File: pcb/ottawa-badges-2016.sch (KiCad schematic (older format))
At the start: 87 parts, among them P1 USB_OTG, P2 CONN_01X08, P3 CONN_01X06, P4 CONN_01X10, P5 CONN_01X08, P6 CONN_02X03, SW1 SWITCH_INV, SW2 SW_PUSH, U1 ATMEGA328P-A, U2 MIC5504-3.3YM5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

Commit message: Started layout of board.
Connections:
- net +3V3: now also P6.6 (P6); no longer P6.2 (P2)
- net DIGITAL12: now also P6.5 (P5); no longer P6.1 (P1)
- net GND: now also P6.2 (P2); no longer P6.6 (P6)
- net RESET: now also P6.1 (P1); no longer P6.5 (P5)
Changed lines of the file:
@@
 F 3 "" H 6750 2300 60  0000 C CNN
 	1    6750 3500
-	1    0    0    -1
+	1    0    0    1
 $EndComp
 $Comp

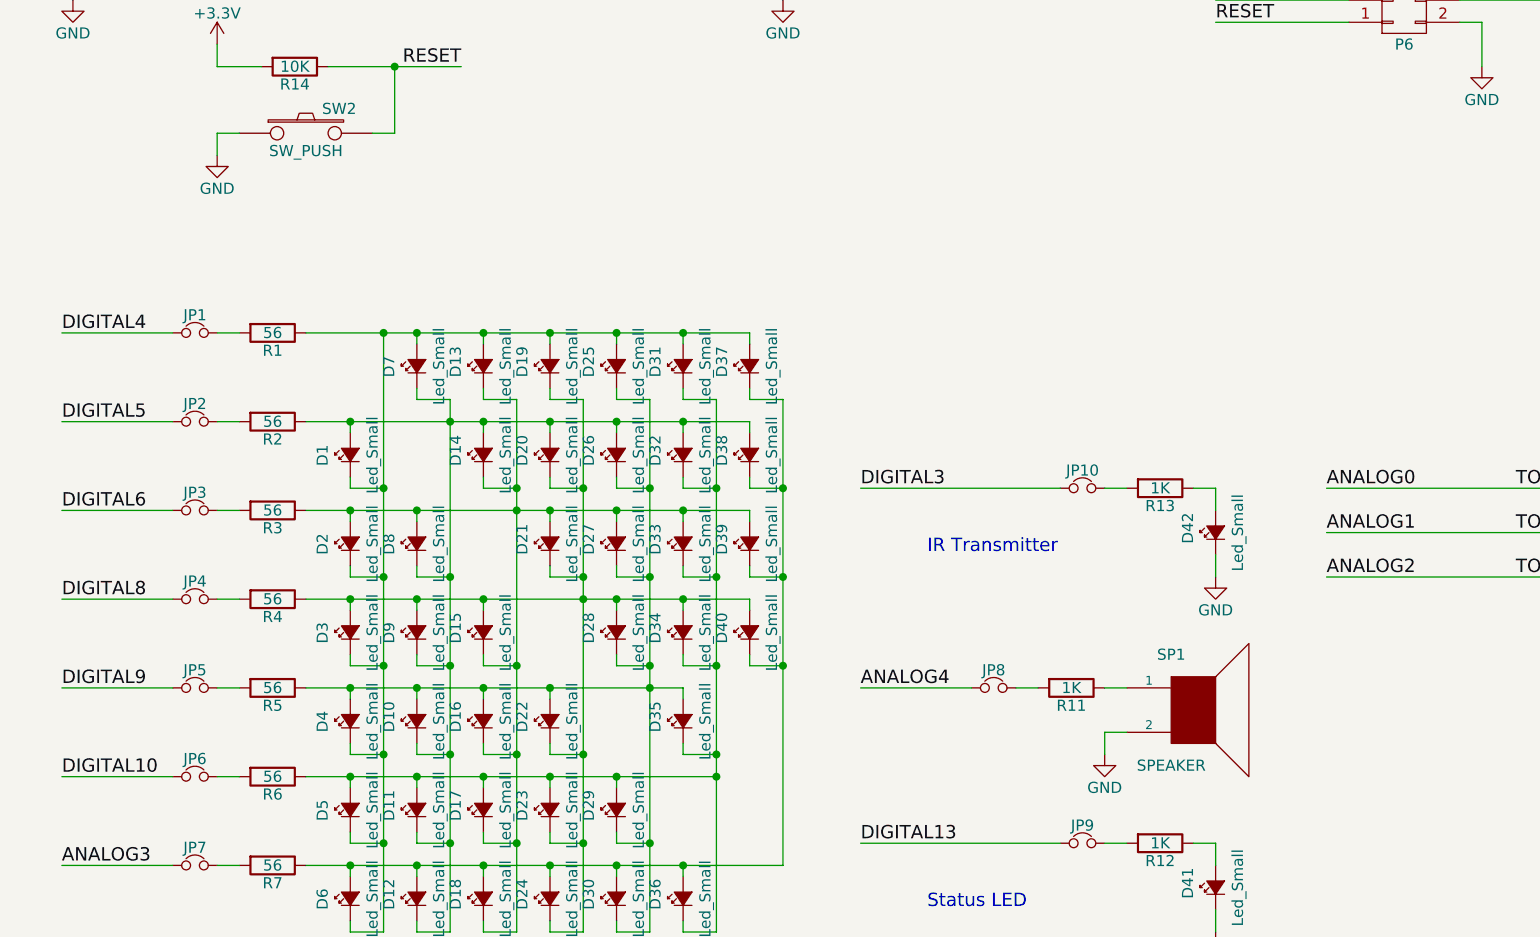
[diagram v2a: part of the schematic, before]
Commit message: MANY CHANGES. Added footprints for USB connector, battery clip, power switch, and solder jumper. Started adding banana jack "sockets".
Need to place the banana jacks, and add the IR receiver and artwork. Then I think we're done for the prototype.
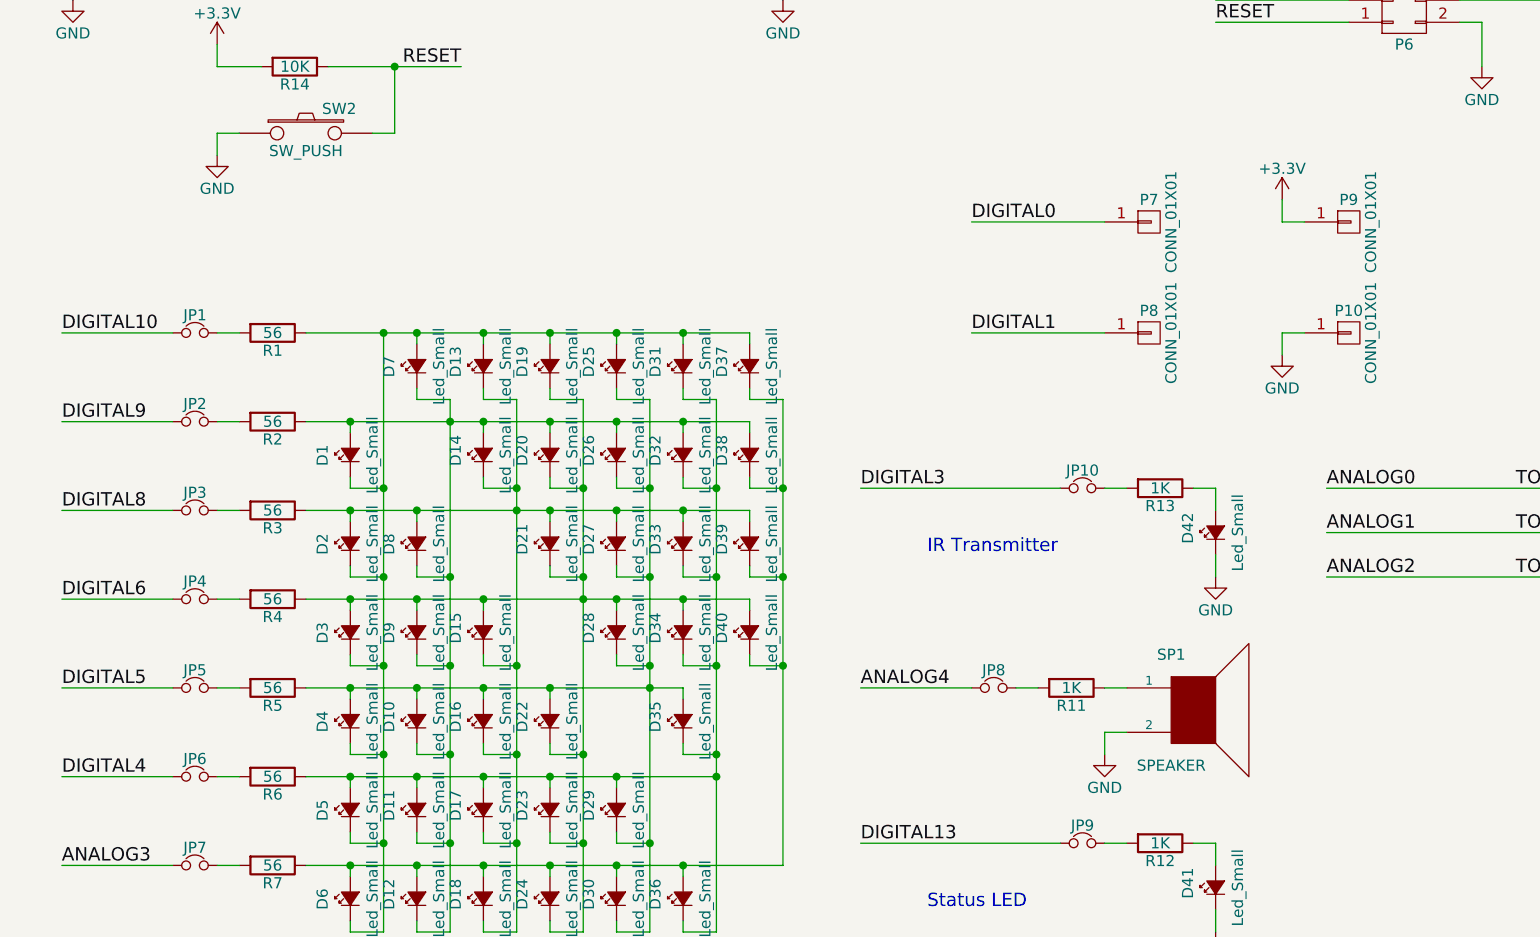
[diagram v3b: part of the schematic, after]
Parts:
- added P10, P7, P8, P9: CONN_01X01, Mounting_Holes:MountingHole_4mm_Pad_Via, symbol CONN_01X01
- BT1: footprint (none) -> BadgeParts:CR2032-SHRAPNEL
- JP1, JP10, JP2, JP3, JP4, JP5, JP6, JP7, JP8, JP9: footprint (none) -> BadgeParts:SJ2
- P1: footprint (none) -> BadgeParts:10118192-0001LF
- SW1: footprint (none) -> BadgeParts:MK-12C02
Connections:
- net +3V3: now also P9.1 (P1)
- net DIGITAL0: now also P7.1 (P1)
- net DIGITAL1: now also P8.1 (P1)
- net DIGITAL10: now also JP1.1; no longer JP6.1
- net DIGITAL4: now also JP6.1; no longer JP1.1
- net DIGITAL5: now also JP5.1; no longer JP2.1
- net DIGITAL6: now also JP4.1; no longer JP3.1
- net DIGITAL8: now also JP3.1; no longer JP4.1
- net DIGITAL9: now also JP2.1; no longer JP5.1
- net GND: now also P10.1 (P1)

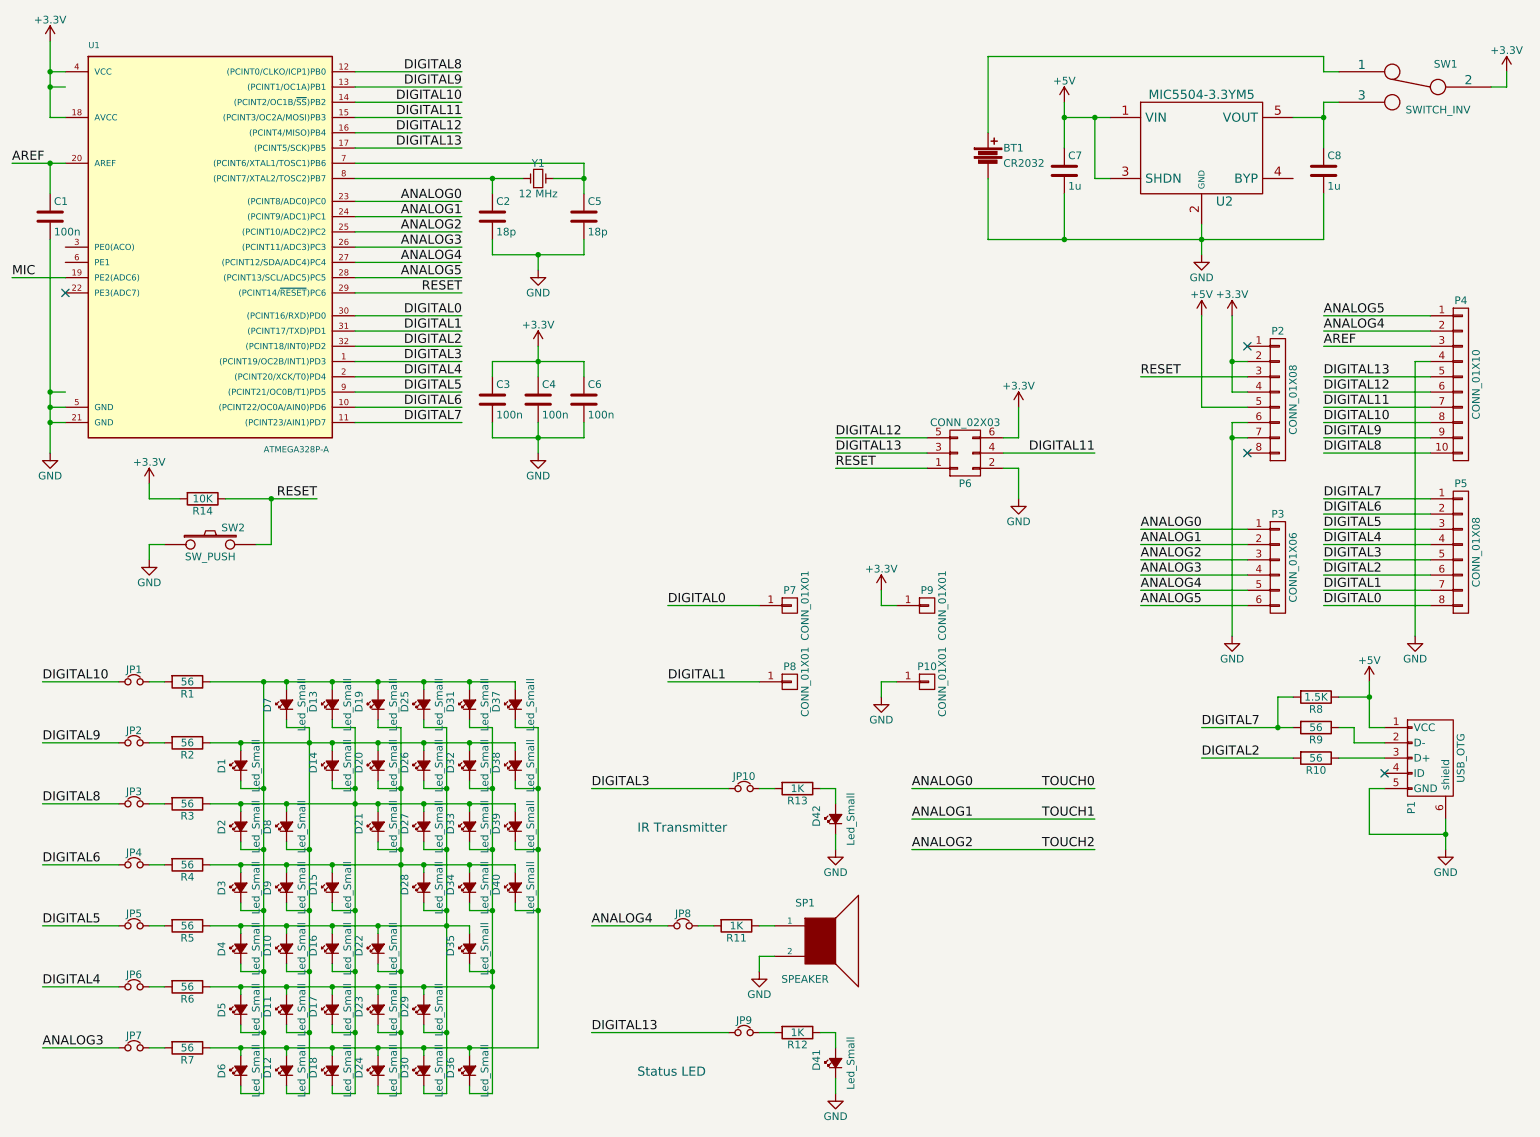
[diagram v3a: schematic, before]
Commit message: Added IR receiver and Maker Faire logo. Still need to add Makey for prototype. Also need to figure out where to put P8 so that it doesn't overlap with the logo.
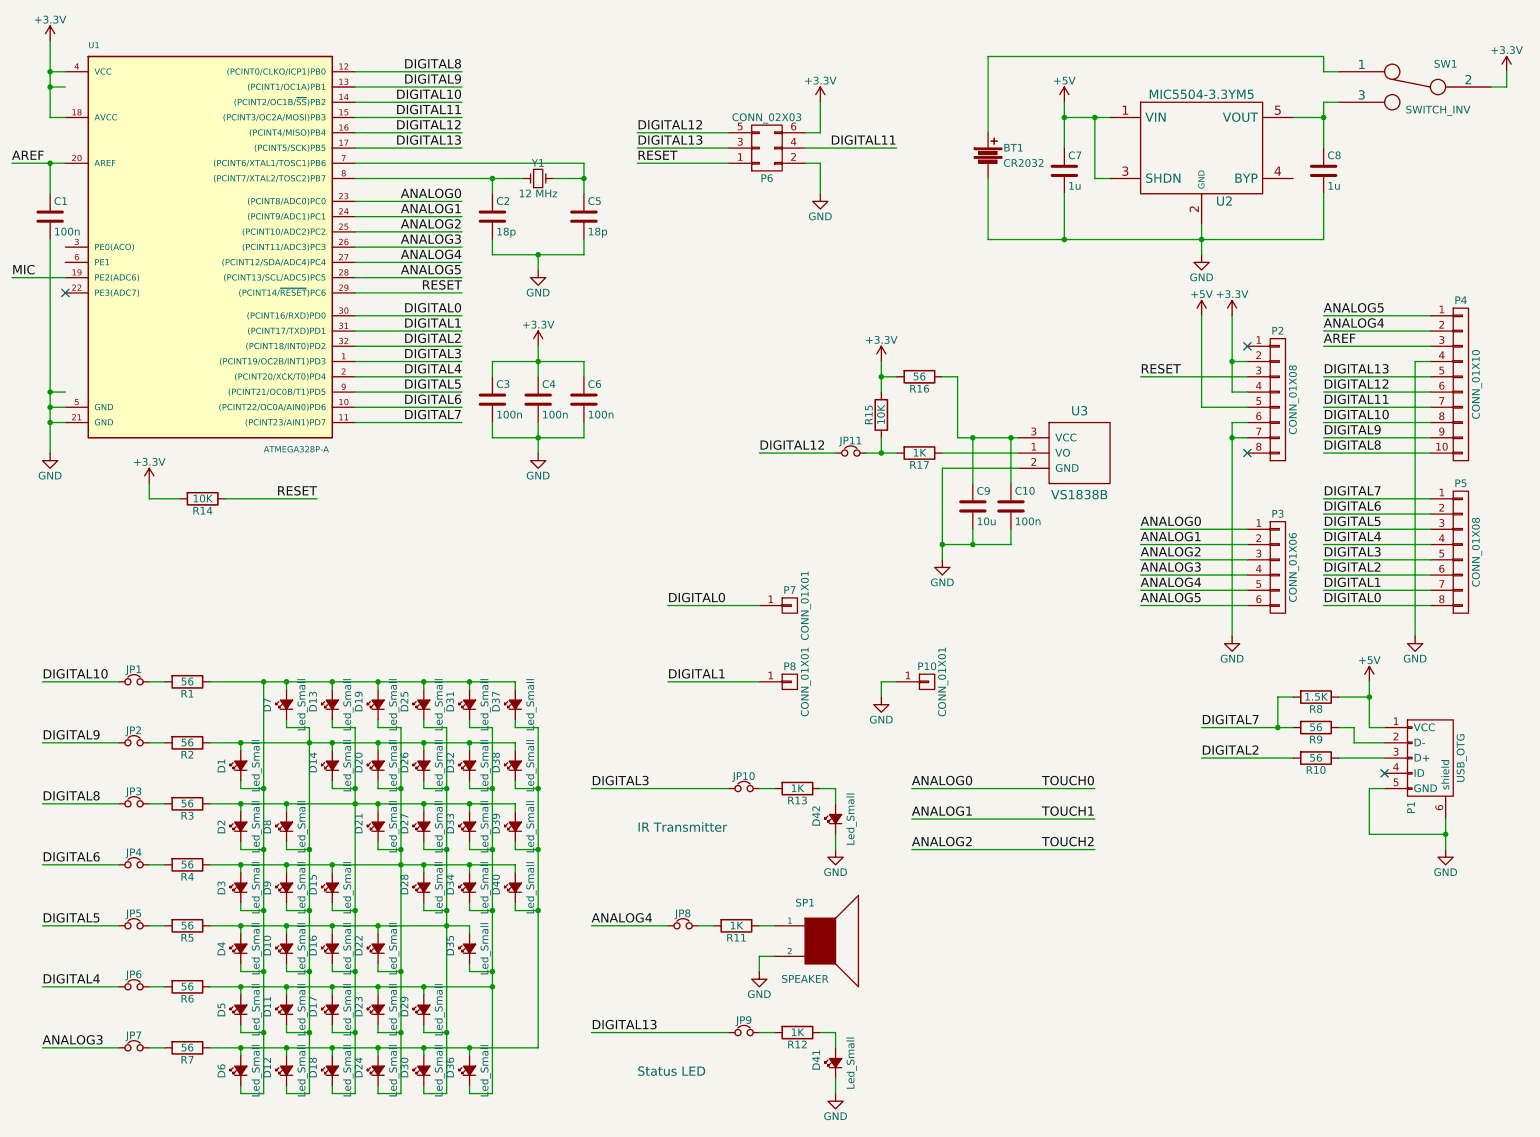
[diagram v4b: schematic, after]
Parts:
- removed P9: CONN_01X01, Mounting_Holes:MountingHole_4mm_Pad_Via, symbol CONN_01X01
- removed SW2: SW_PUSH, Buttons_Switches_SMD:SW_SPST_FSMSM, symbol SW_PUSH
- added C10: 100n, Capacitors_SMD:C_0603, symbol C
- added C9: 10u, Capacitors_SMD:C_0805, symbol C
- added JP11: Jumper_NC_Small, BadgeParts:SJ2, symbol Jumper_NC_Small
- added R15: 10K, Resistors_SMD:R_0603, symbol R
- added R16: 56, Resistors_SMD:R_0603, symbol R
- added R17: 1K, Resistors_SMD:R_0603, symbol R
- added U3: VS1838B, BadgeParts:VS1838B-HORIZ, symbol VS1838B
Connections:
- net +3V3: now also R15.2, R16.2
- net DIGITAL12: now also JP11.1
- net GND: now also C10.2, C9.2, U3.2 (GND)
- new net: R17.1, U3.1 (VO)
- new net: C10.1, C9.1, R16.1, U3.3 (VCC)
- new net: JP11.2, R15.1, R17.2
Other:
- moved on the sheet: P6

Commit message: Adding latest files from ATMega328PB version and BOM.
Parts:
- removed C3: 100n, Capacitors_SMD:C_0603, symbol C
- added P9: CONN_01X04, Socket_Strips:Socket_Strip_Straight_1x04, symbol CONN_01X04
- U1: symbol ATMEGA328P-A -> ATMEGA328PB-A
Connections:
- net PE3: now reaches U1.22 (PE3(ADC7))
- net PE3: now also P9.4 (P4)
- net PE0: now reaches U1.3 (PE0(ACO))
- net PE0: now also P9.1 (P1)
- net PE1: now reaches U1.6 (PE1)
- net PE1: now also P9.2 (P2)
- net MIC renamed PE2
- net PE2: now also P9.3 (P3)
- no-connect marks 4 -> 3
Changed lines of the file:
@@
 $EndDescr
 $Comp
-L ATMEGA328P-A U1
+L ATMEGA328PB-A U1
 U 1 1 575E45D7
 P 1750 2100
@@
 $EndComp
 $Comp
-L C C3
-U 1 1 575F02FB
-P 3650 3150
-F 0 "C3" H 3675 3250 50  0000 L CNN
-F 1 "100n" H 3675 3050 50  0000 L CNN
-F 2 "Capacitors_SMD:C_0603" H 3688 3000 30  0001 C CNN
-F 3 "" H 3650 3150 60  0000 C CNN
-	1    3650 3150
-	1    0    0    -1
-$EndComp
-$Comp
 L C C4
 U 1 1 575F038C
@@
 	2750 2450 3450 2450
 Wire Wire Line
-	850  3100 750  3100
-Wire Wire Line
 	750  2100 750  3500
 Wire Wire Line
@@
 Wire Wire Line
 	750  800  750  1300
-Wire Wire Line
-	850  1100 750  1100
-Connection ~ 750  1100
 Wire Wire Line
 	850  1000 750  1000
@@
 	3950 2800 3950 3000
 Wire Wire Line
-	3650 2900 4250 2900
-Wire Wire Line
-	3650 2900 3650 3000
-Wire Wire Line
-	3650 3300 3650 3400
-Wire Wire Line
-	3650 3400 4250 3400
-Wire Wire Line
 	3950 3300 3950 3500
 Wire Wire Line
@@
 Wire Wire Line
 	750  1600 750  1800
-Connection ~ 750  3100
 Wire Wire Line
 	9500 5400 9300 5400
@@
 NoConn ~ 9500 5600
 Text Label 500  2350 0    60   ~ 0
-MIC
+PE2
 Wire Wire Line
 	500  2350 850  2350
-NoConn ~ 850  2450
 $Comp
 L CONN_01X01 P7
@@
 $EndComp
 $Comp
-L GND #PWR022
+L GND #PWR021
 U 1 1 5768DC08
 P 6200 5100
-F 0 "#PWR022" H 6200 4850 50  0001 C CNN
+F 0 "#PWR021" H 6200 4850 50  0001 C CNN
 F 1 "GND" H 6200 4950 50  0000 C CNN
 F 2 "" H 6200 5100 60  0000 C CNN
@@
 $EndComp
 $Comp
-L GND #PWR023
+L GND #PWR022
 U 1 1 576D5F67
 P 6600 4200
-F 0 "#PWR023" H 6600 3950 50  0001 C CNN
+F 0 "#PWR022" H 6600 3950 50  0001 C CNN
 F 1 "GND" H 6600 4050 50  0000 C CNN
 F 2 "" H 6600 4200 60  0000 C CNN
@@
 Connection ~ 6800 4100
 $Comp
-L +3.3V #PWR024
+L +3.3V #PWR023
 U 1 1 576DFC08
 P 6200 2900
-F 0 "#PWR024" H 6200 2750 50  0001 C CNN
+F 0 "#PWR023" H 6200 2750 50  0001 C CNN
 F 1 "+3.3V" H 6200 3040 50  0000 C CNN
 F 2 "" H 6200 2900 60  0000 C CNN
@@
 	6700 3000 6700 3400
 Connection ~ 6800 3400
+Text Label 500  2250 0    60   ~ 0
+PE1
+Text Label 500  2150 0    60   ~ 0
+PE0
+Text Label 500  2450 0    60   ~ 0
+PE3
+Wire Wire Line
+	500  2450 850  2450
+Wire Wire Line
+	500  2250 850  2250
+Wire Wire Line
+	850  2150 500  2150
+$Comp
+L CONN_01X04 P9
+U 1 1 57E9B5A1
+P 3700 4450
+F 0 "P9" H 3700 4700 50  0000 C CNN
+F 1 "CONN_01X04" V 3800 4450 50  0000 C CNN
+F 2 "Socket_Strips:Socket_Strip_Straight_1x04" H 3700 4450 60  0001 C CNN
+F 3 "" H 3700 4450 60  0000 C CNN
+	1    3700 4450
+	1    0    0    -1
+$EndComp
+Wire Wire Line
+	3500 4600 3000 4600
+Wire Wire Line
+	3000 4500 3500 4500
+Wire Wire Line
+	3500 4400 3000 4400
+Wire Wire Line
+	3000 4300 3500 4300
+Text Label 3000 4300 0    60   ~ 0
+PE0
+Text Label 3000 4400 0    60   ~ 0
+PE1
+Text Label 3000 4500 0    60   ~ 0
+PE2
+Text Label 3000 4600 0    60   ~ 0
+PE3
+Wire Wire Line
+	4250 2900 3950 2900
+Wire Wire Line
+	3950 3400 4250 3400
 $EndSCHEMATC
